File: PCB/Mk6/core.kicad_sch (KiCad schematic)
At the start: 12 parts, among them J2 Bank, J25 Debug, U3 GAL20V8B-10, U4 R65C02, U5 EEPROM, U8 62256

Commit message: save point
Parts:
- added U27: 74LS138, symbol 74xx:74LS138
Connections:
- net ~{PORT} is gone; now on net ~{RD}: RN25.5 (R4), U3.19 (I/O/Q4)
- net +5V: now also U27.16 (VCC), U27.6 (E3)
- net A4: now also U27.1 (A0)
- net A5: now also U27.2 (A1)
- net A6: now also U27.3 (A2)
- net A7: now also U27.5 (E2)
- net DISP: now also RN25.7 (R6), U3.17 (I/O/Q6); no longer RN25.4 (R3), U3.20 (I/O/Q3)
- net GND: now also U27.8 (GND)
- net ~{COM}: now also U27.15 (O0); no longer RN25.8 (R7), U3.16 (I/O/Q7)
- net ~{RD}: no longer RN25.7 (R6), U3.17 (I/O/Q6)
- net ~{VIA}: now also U27.14 (O1); no longer RN25.9 (R8), U3.15 (I/O/Q8)
- net ~{WR}: now also RN25.4 (R3), U3.20 (I/O/Q3); no longer RN25.6 (R5), U3.18 (I/O/Q5)
- new net ~{IO}: RN25.6 (R5), U27.4 (E1), U3.18 (I/O/Q5)
- new net ~{KEY}: RN25.8 (R7), U3.16 (I/O/Q7)
- new net ~{OUT}: RN25.9 (R8), U3.15 (I/O/Q8)
- new net ~{PORT2}: U27.13 (O2)
- new net ~{PORT3}: U27.12 (O3)
- new net ~{PORT4}: U27.11 (O4)
- new net ~{PORT5}: U27.10 (O5)
- new net ~{PORT6}: U27.9 (O6)
- new net ~{PORT7}: U27.7 (O7)

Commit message: save
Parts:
- J4: renamed from J25; footprint (none) -> Connector_PinHeader_2.54mm:PinHeader_1x08_P2.54mm_Vertical
- JP3: renamed from JP28; footprint Jumper:SolderJumper-2_P1.3mm_Bridged_RoundedPad1.0x1.5mm -> Connector_PinHeader_2.54mm:PinHeader_1x02_P2.54mm_Vertical
- U7: renamed from U27; footprint (none) -> Package_DIP:DIP-16_W7.62mm_LongPads
- renumbered J2 to J3, JP26 to JP2, JP25 to JP4, RN25 to RN2, RP1 to RP2, RP2 to RP3, U8 to U6, U3 to U8
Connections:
- net ~{KEY} is gone; now on net ~{IO}: RN2.8 (R7), U8.16 (I/O/Q7)
- net BA0: now also J3.4 (Pin_4); no longer J3.1 (Pin_1)
- net BA1: now also J3.3 (Pin_3), RP3.4 (R3); no longer J3.2 (Pin_2), RP3.3 (R2)
- net BA2: now also J3.2 (Pin_2), RP3.3 (R2); no longer J3.3 (Pin_3), RP3.4 (R3)
- net BA3: now also J3.1 (Pin_1), RP3.2 (R1); no longer J3.4 (Pin_4), RP3.5 (R4)
- net Clk0: now also RN2.9 (R8), U8.15 (I/O/Q8); no longer RN2.2 (R1), U8.22 (I/O/Q1)
- net Clk2: now also U8.14 (In11)
- net R~{W}: now also U8.10 (In09); no longer U8.14 (In11)
- net ~{IO}: no longer RN2.6 (R5), U8.18 (I/O/Q5)
- net ~{OUT}: now also RN2.2 (R1), U8.22 (I/O/Q1); no longer RN2.9 (R8), U8.15 (I/O/Q8)
- net ~{RD}: now also RN2.6 (R5), U8.18 (I/O/Q5), U8.6 (In05); no longer RN2.5 (R4), U8.19 (I/O/Q4)
- net ~{WR}: now also RN2.5 (R4), U8.19 (I/O/Q4); no longer RN2.4 (R3), U8.20 (I/O/Q3)
- net at JP3.2 (B): now also RP3.5 (R4); no longer RP3.2 (R1)
- net ~{PORT2} renamed ~{SLOT2}
- net ~{PORT3} renamed ~{SLOT3}
- net ~{PORT4} renamed ~{SLOT4}
- net ~{PORT5} renamed ~{SLOT5}
- net ~{PORT6} renamed ~{SLOT6}
- net ~{PORT7} renamed ~{SLOT7}
- net ~{SO}: no longer names the net of RP2.3 (R2), U4.38 (~{SO})
- new net ~{IN}: RN2.4 (R3), U8.20 (I/O/Q3)
- no-connect marks 8 -> 3
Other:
- moved on the sheet: J3

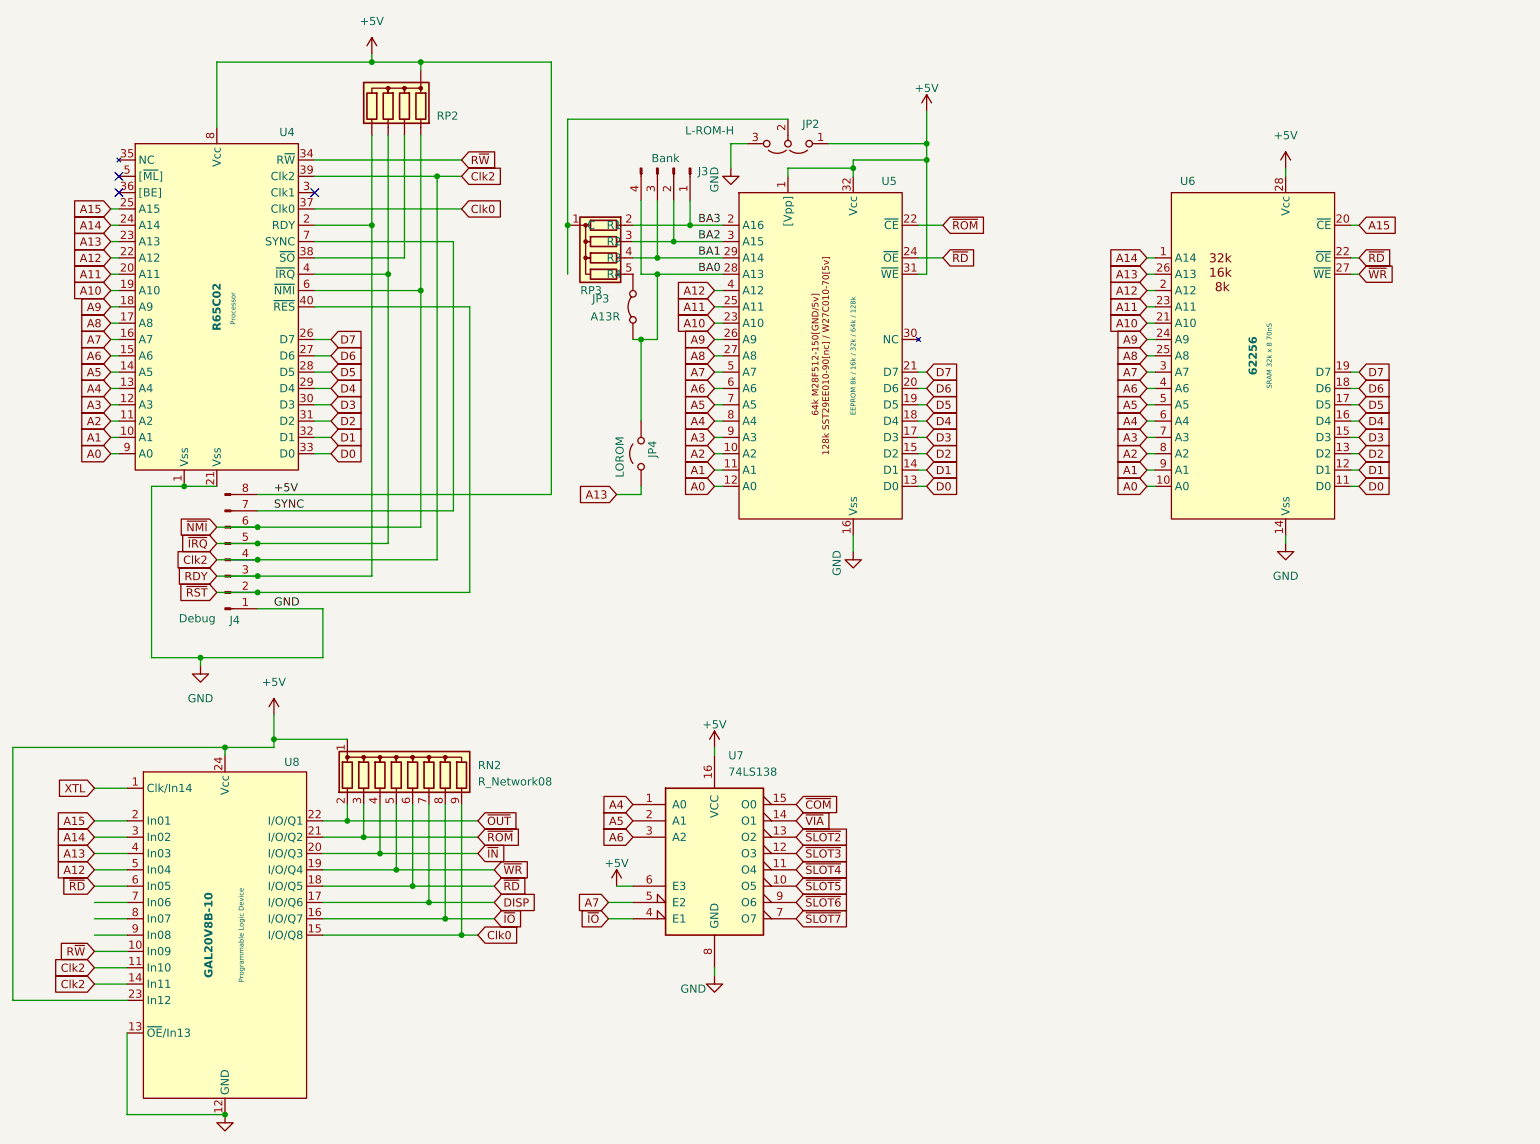
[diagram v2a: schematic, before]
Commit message: all done, pre-clk div
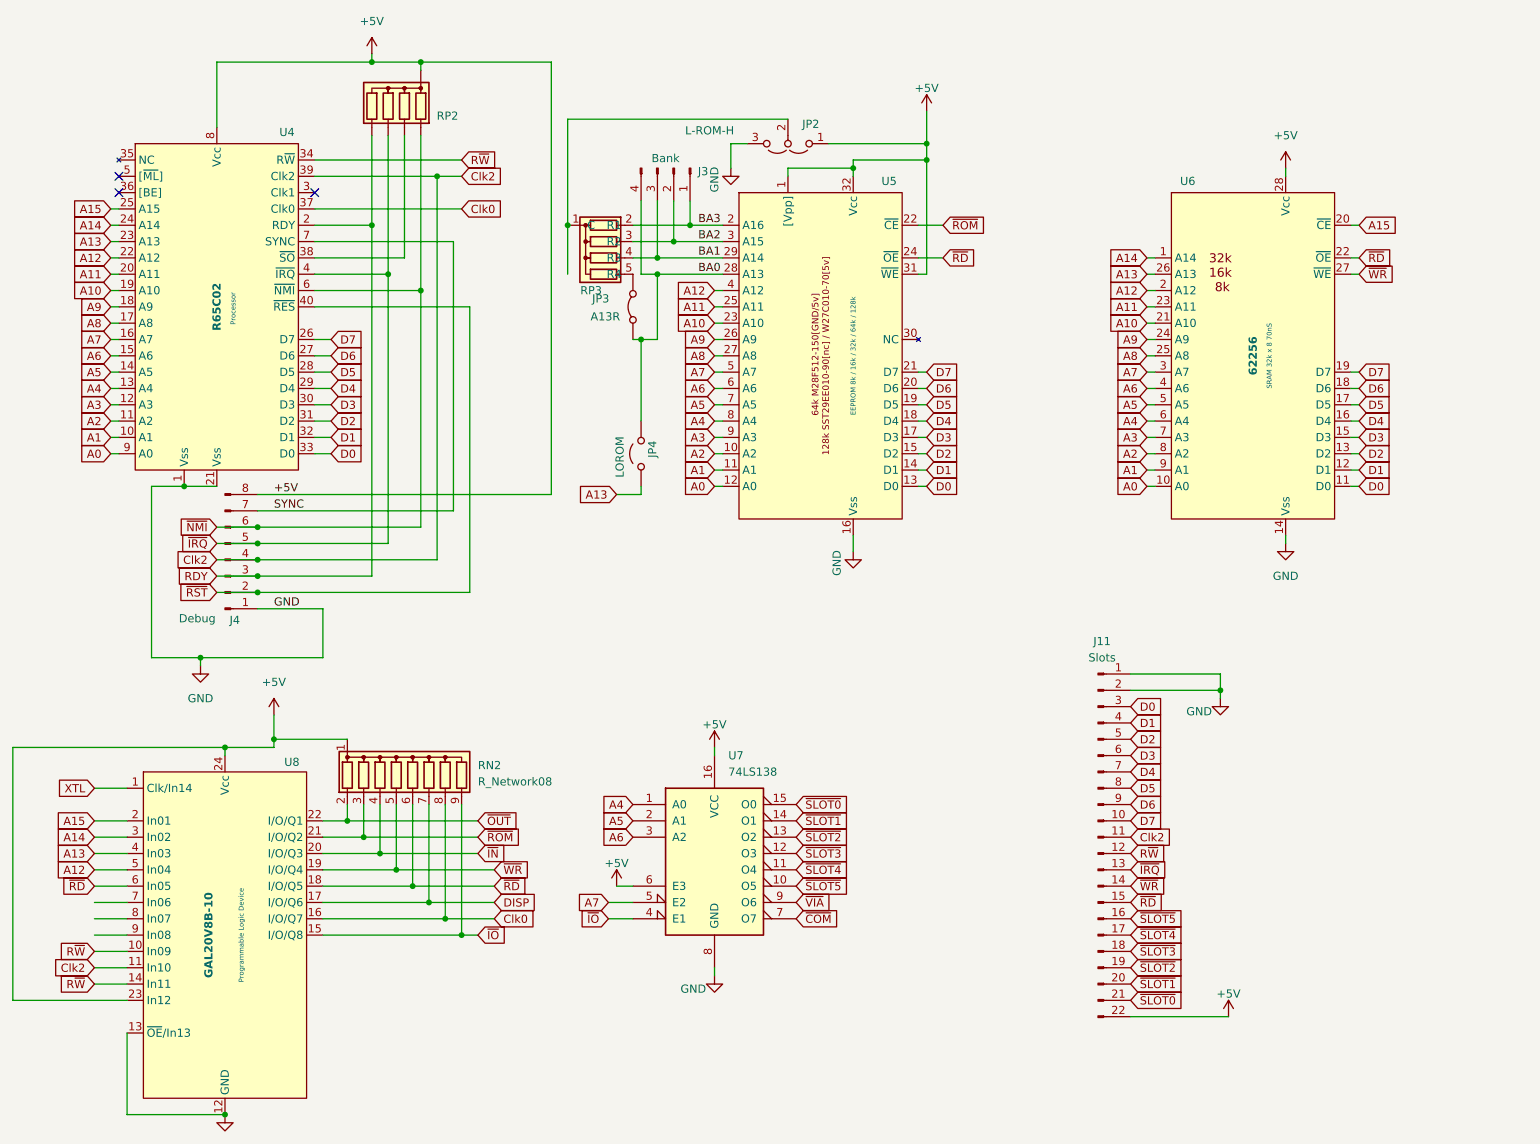
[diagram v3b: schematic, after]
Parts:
- added J11: Slots, Connector_PinHeader_2.54mm:PinHeader_1x22_P2.54mm_Vertical, symbol Connector:Conn_01x22_Pin
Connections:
- net ~{SLOT6} is gone; now on net ~{VIA}: U7.9 (O6)
- net ~{SLOT7} is gone; now on net ~{COM}: U7.7 (O7)
- net +5V: now also J11.22 (Pin_22)
- net Clk0: now also RN2.8 (R7), U8.16 (I/O/Q7); no longer RN2.9 (R8), U8.15 (I/O/Q8)
- net Clk2: now also J11.11 (Pin_11); no longer U8.14 (In11)
- net D0: now also J11.3 (Pin_3)
- net D1: now also J11.4 (Pin_4)
- net D2: now also J11.5 (Pin_5)
- net D3: now also J11.6 (Pin_6)
- net D4: now also J11.7 (Pin_7)
- net D5: now also J11.8 (Pin_8)
- net D6: now also J11.9 (Pin_9)
- net D7: now also J11.10 (Pin_10)
- net GND: now also J11.1 (Pin_1), J11.2 (Pin_2)
- net R~{W}: now also U8.14 (In11), J11.12 (Pin_12)
- net ~{COM}: no longer U7.15 (O0)
- net ~{IO}: now also RN2.9 (R8), U8.15 (I/O/Q8); no longer RN2.8 (R7), U8.16 (I/O/Q7)
- net ~{IRQ}: now also J11.13 (Pin_13)
- net ~{RD}: now also J11.15 (Pin_15)
- net ~{SLOT2}: now also J11.19 (Pin_19)
- net ~{SLOT3}: now also J11.18 (Pin_18)
- net ~{SLOT4}: now also J11.17 (Pin_17)
- net ~{SLOT5}: now also J11.16 (Pin_16)
- net ~{VIA}: no longer U7.14 (O1)
- net ~{WR}: now also J11.14 (Pin_14)
- new net ~{SLOT0}: J11.21 (Pin_21), U7.15 (O0)
- new net ~{SLOT1}: J11.20 (Pin_20), U7.14 (O1)

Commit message: Cleaned
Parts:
- removed J11: Slots, Connector_PinHeader_2.54mm:PinHeader_1x22_P2.54mm_Vertical, symbol Connector:Conn_01x22_Pin
- removed JP3: A13R, Connector_PinHeader_2.54mm:PinHeader_1x02_P2.54mm_Vertical, symbol Jumper:Jumper_2_Bridged
- removed JP4: LOROM, Connector_PinHeader_2.54mm:PinHeader_1x02_P2.54mm_Vertical, symbol RetroParts_Library:Jumper_2_Open
- removed U7: 74LS138, Package_DIP:DIP-16_W7.62mm_LongPads, symbol 74xx:74LS138
- added JP8: 16-k-8, Connector_PinHeader_2.54mm:PinHeader_1x03_P2.54mm_Vertical, symbol Jumper:Jumper_3_Open
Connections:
- net XTL is gone; now on net Clk2: U8.1 (Clk/In14)
- net ~{IO} is gone; now on net ~{COM}: RN2.9 (R8), U8.15 (I/O/Q8)
- net A10: now also U8.8 (In07)
- net A11: now also U8.9 (In08)
- net A13: now also JP8.1 (A)
- net A9: now also U8.7 (In06)
- net BA0: now also JP8.2 (C)
- net Clk0: no longer RN2.8 (R7), U8.16 (I/O/Q7)
- net DISP: now also RN2.5 (R4), U8.19 (I/O/Q4); no longer RN2.7 (R6), U8.17 (I/O/Q6)
- net ~{VIA}: now also RN2.8 (R7), U8.16 (I/O/Q7)
- net ~{WR}: now also RN2.7 (R6), U8.17 (I/O/Q6); no longer RN2.5 (R4), U8.19 (I/O/Q4)
- net at RP3.5 (R4): now also JP8.3 (B)
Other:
- note added: "0000-7FFF !A15 -> RAM 32K C000-FFFF !ROM (16k) BE00-BFFF !COM BC00-BDFF !VIA BA00-BBFF IN/OUT B000 B800 8000-AFFF DISP"

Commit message: Pre Remap
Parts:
- removed J4: Debug, Connector_PinHeader_2.54mm:PinHeader_1x08_P2.54mm_Vertical, symbol Connector:Conn_01x08_Pin
- added J4: Debug, Connector_PinHeader_2.54mm:PinHeader_1x09_P2.54mm_Vertical, symbol Connector_Generic:Conn_01x09
- JP2: value L-ROM-H -> Up-PULL-Down
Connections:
- net +5V: now also J4.9 (Pin_9)
- net Clk0: now also J4.6 (Pin_6)
- net Clk2: now also J4.4 (Pin_4)
- net GND: now also J4.1 (Pin_1)
- net RDY: now also J4.3 (Pin_3)
- net SYNC: now also J4.8 (Pin_8)
- net ~{IRQ}: now also J4.5 (Pin_5)
- net ~{NMI}: now also J4.7 (Pin_7)
- net ~{RST}: now also J4.2 (Pin_2)

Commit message: Added 3-8 IO, extra GAL out, attachment point for !RAM
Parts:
- added J12: ~{RAM} A15, Connector_PinHeader_2.54mm:PinHeader_1x02_P2.54mm_Vertical, symbol RetroParts_Library:Jumper_2_Open
- added J5: IO:[0,1,2,3,4,5] EXT, Connector_PinSocket_2.54mm:PinSocket_1x07_P2.54mm_Vertical, symbol Connector:Conn_01x07_Pin
- added U8: 74LS138, Package_DIP:DIP-16_W7.62mm_LongPads, symbol 74xx:74LS138
- renumbered JP2 to JP4, JP8 to JP5, U4 to U5, U5 to U6, U6 to U7, U8 to U9
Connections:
- net +5V: now also U8.16 (VCC)
- net A10: now also U8.2 (A1)
- net A11: now also U8.3 (A2)
- net A15: now also J12.2 (B); no longer U7.20 (~{CE})
- net A9: now also U8.1 (A0)
- net DISP: now also RN2.9 (R8), U9.15 (I/O/Q8); no longer RN2.5 (R4), U9.19 (I/O/Q4)
- net GND: now also U8.4 (E1), U8.5 (E2), U8.8 (GND)
- net ~{COM}: now also U8.7 (O7); no longer RN2.9 (R8), U9.15 (I/O/Q8)
- net ~{RD}: now also RN2.7 (R6), U9.17 (I/O/Q6); no longer RN2.6 (R5), U9.18 (I/O/Q5)
- net ~{VIA}: now also U8.9 (O6); no longer RN2.8 (R7), U9.16 (I/O/Q7)
- net ~{WR}: now also RN2.8 (R7), U9.16 (I/O/Q7); no longer RN2.7 (R6), U9.17 (I/O/Q6)
- new net: J12.1 (A), U7.20 (~{CE})
- new net EXT: J5.7 (Pin_7), RN2.5 (R4), U9.19 (I/O/Q4)
- new net IO: RN2.6 (R5), U8.6 (E3), U9.18 (I/O/Q5)
- new net ~{IO0}: J5.1 (Pin_1), U8.15 (O0)
- new net ~{IO1}: J5.2 (Pin_2), U8.14 (O1)
- new net ~{IO2}: J5.3 (Pin_3), U8.13 (O2)
- new net ~{IO3}: J5.4 (Pin_4), U8.12 (O3)
- new net ~{IO4}: J5.5 (Pin_5), U8.11 (O4)
- new net ~{IO5}: J5.6 (Pin_6), U8.10 (O5)

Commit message: cleanup
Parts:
- J3: value Bank -> Bank:3..0
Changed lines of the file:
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@@
 			)
 		)
-		(property "Value" "Bank"
+		(property "Value" "Bank:3..0"
 			(at 130.81 41.656 90)
 			(effects
